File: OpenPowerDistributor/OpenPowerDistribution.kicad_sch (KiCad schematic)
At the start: 0 parts

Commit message: Started to draw schematic
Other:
- added sheet 24V boost (24V boost.kicad_sch)
- added sheet 3.3V internal supply (3.3V internal supply.kicad_sch)
- added sheet 30V Gate power (30V Gate power.kicad_sch)
- added sheet 5V buck converter (5V buck converter.kicad_sch)
- added sheet Power input (Power input.kicad_sch)
- note added: "30V power supply for high-side FET gate power"
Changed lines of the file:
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@@
 (kicad_sch (version 20230121) (generator eeschema)
   (paper "A4")
+  (text "30V power supply for high-side FET gate power" (at 54.61 24.13 0)
+    (effects (font (size 3 3)) (justify left bottom))
+  )
+  (sheet (at 77.47 52.07) (size 40.64 13.97) (fields_autoplaced)
+    (stroke (width 0.1524) (type solid))
+    (fill (color 0 0 0 0.0000))
+    (property "Sheetname" "24V boost" (at 77.47 51.3584 0)
+      (effects (font (size 1.27 1.27)) (justify left bottom))
+    )
+    (property "Sheetfile" "24V boost.kicad_sch" (at 77.47 66.6246 0)
+      (effects (font (size 1.27 1.27)) (justify left top))
+    )
+    (instances
+      (project "OpenPowerDistribution"
+        (path "/df87b081-37a2-452c-8581-7eff2c408a17" (page "6"))
+      )
+    )
+  )
+  (sheet (at 77.47 34.29) (size 40.64 11.43) (fields_autoplaced)
+    (stroke (width 0.1524) (type solid))
+    (fill (color 0 0 0 0.0000))
+    (property "Sheetname" "30V Gate power" (at 77.47 33.5784 0)
+      (effects (font (size 1.27 1.27)) (justify left bottom))
+    )
+    (property "Sheetfile" "30V Gate power.kicad_sch" (at 77.47 46.3046 0)
+      (effects (font (size 1.27 1.27)) (justify left top))
+    )
+    (instances
+      (project "OpenPowerDistribution"
+        (path "/df87b081-37a2-452c-8581-7eff2c408a17" (page "5"))
+      )
+    )
+  )
+  (sheet (at 77.47 93.98) (size 40.64 11.43) (fields_autoplaced)
+    (stroke (width 0.1524) (type solid))
+    (fill (color 0 0 0 0.0000))
+    (property "Sheetname" "3.3V internal supply" (at 77.47 93.2684 0)
+      (effects (font (size 1.27 1.27)) (justify left bottom))
+    )
+    (property "Sheetfile" "3.3V internal supply.kicad_sch" (at 77.47 105.9946 0)
+      (effects (font (size 1.27 1.27)) (justify left top))
+    )
+    (instances
+      (project "OpenPowerDistribution"
+        (path "/df87b081-37a2-452c-8581-7eff2c408a17" (page "4"))
+      )
+    )
+  )
+  (sheet (at 38.1 34.29) (size 29.21 11.43) (fields_autoplaced)
+    (stroke (width 0.1524) (type solid))
+    (fill (color 0 0 0 0.0000))
+    (property "Sheetname" "Power input" (at 38.1 33.5784 0)
+      (effects (font (size 1.27 1.27)) (justify left bottom))
+    )
+    (property "Sheetfile" "Power input.kicad_sch" (at 38.1 46.3046 0)
+      (effects (font (size 1.27 1.27)) (justify left top))
+    )
+    (instances
+      (project "OpenPowerDistribution"
+        (path "/df87b081-37a2-452c-8581-7eff2c408a17" (page "2"))
+      )
+    )
+  )
+  (sheet (at 77.47 73.66) (size 40.64 11.43) (fields_autoplaced)
+    (stroke (width 0.1524) (type solid))
+    (fill (color 0 0 0 0.0000))
+    (property "Sheetname" "5V buck converter" (at 77.47 72.9484 0)
+      (effects (font (size 1.27 1.27)) (justify left bottom))
+    )
+    (property "Sheetfile" "5V buck converter.kicad_sch" (at 77.47 85.6746 0)
+      (effects (font (size 1.27 1.27)) (justify left top))
+    )
+    (instances
+      (project "OpenPowerDistribution"
+        (path "/df87b081-37a2-452c-8581-7eff2c408a17" (page "3"))
+      )
+    )
+  )
   (sheet_instances
     (path "/" (page "1"))

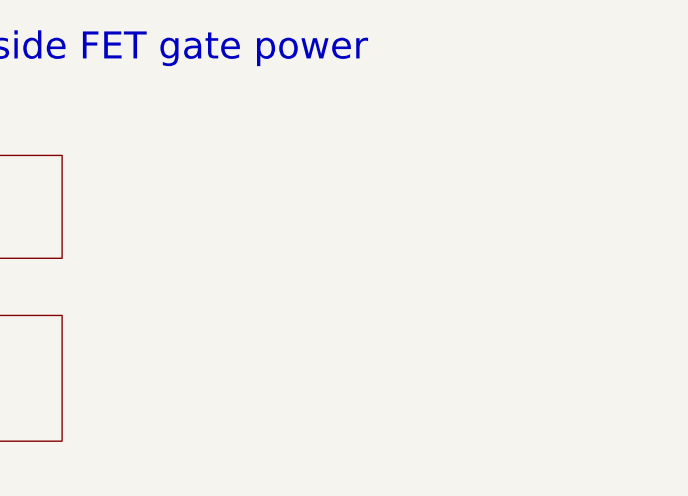
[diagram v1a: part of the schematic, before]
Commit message: Added manual high side power switch
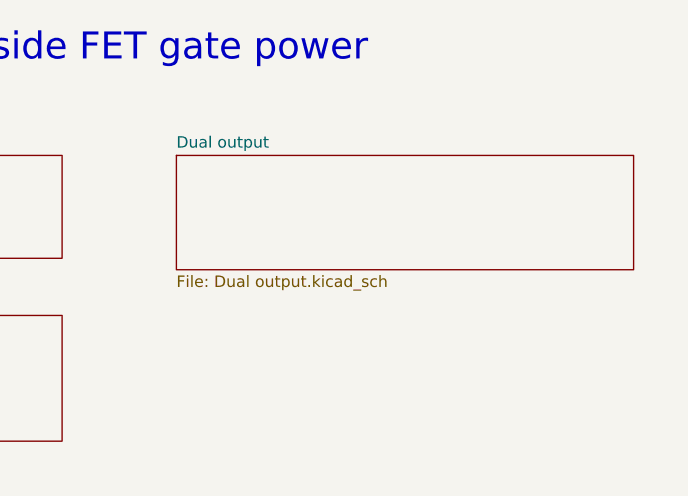
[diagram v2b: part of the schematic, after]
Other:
- added sheet Dual output (Dual output.kicad_sch)
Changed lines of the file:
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@@
+    )
+  )
+  (sheet (at 130.81 34.29) (size 50.8 12.7) (fields_autoplaced)
+    (stroke (width 0.1524) (type solid))
+    (fill (color 0 0 0 0.0000))
+    (property "Sheetname" "Dual output" (at 130.81 33.5784 0)
+      (effects (font (size 1.27 1.27)) (justify left bottom))
+    )
+    (property "Sheetfile" "Dual output.kicad_sch" (at 130.81 47.5746 0)
+      (effects (font (size 1.27 1.27)) (justify left top))
+    )
+    (instances
+      (project "OpenPowerDistribution"
+        (path "/df87b081-37a2-452c-8581-7eff2c408a17" (page "7"))
+      )
     )
   )

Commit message: More schematic progress
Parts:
- added D2 (x4): SMAJ9.0A, Diode_SMD:D_SMA, symbol Diode:SMAJ12A
- added D2 (x6): SMAJ5.0A, Diode_SMD:D_SMA, symbol Diode:SMAJ12A
- added D2 (x6): SMAJ12A, Diode_SMD:D_SMA, symbol Diode:SMAJ12A
- added D2 (x2): SMAJ24A, Diode_SMD:D_SMA, symbol Diode:SMAJ12A
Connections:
- new net Dual output/O1+: D2.1 (A1)
- new net Dual output/O1-: D2.2 (A2)
- new net Dual output/O2+: D2.1 (A1)
- new net Dual output/O2-: D2.2 (A2)
- new net Dual output1/O1+: D2.1 (A1)
- new net Dual output1/O1-: D2.2 (A2)
- new net Dual output1/O2+: D2.1 (A1)
- new net Dual output1/O2-: D2.2 (A2)
- new net Dual output2/O1+: D2.1 (A1)
- new net Dual output2/O1-: D2.2 (A2)
- new net Dual output2/O2+: D2.1 (A1)
- new net Dual output2/O2-: D2.2 (A2)
- new net Dual output3/O1+: D2.1 (A1)
- new net Dual output3/O1-: D2.2 (A2)
- new net Dual output3/O2+: D2.1 (A1)
- new net Dual output3/O2-: D2.2 (A2)
- new net Dual output4/O1+: D2.1 (A1)
- new net Dual output4/O1-: D2.2 (A2)
- new net Dual output4/O2+: D2.1 (A1)
- new net Dual output4/O2-: D2.2 (A2)
- new net Dual output5/O1+: D2.1 (A1)
- new net Dual output5/O1-: D2.2 (A2)
- new net Dual output5/O2+: D2.1 (A1)
- new net Dual output5/O2-: D2.2 (A2)
- new net Dual output6/O1+: D2.1 (A1)
- new net Dual output6/O1-: D2.2 (A2)
- new net Dual output6/O2+: D2.1 (A1)
- new net Dual output6/O2-: D2.2 (A2)
- new net Dual output7/O1+: D2.1 (A1)
- new net Dual output7/O1-: D2.2 (A2)
- new net Dual output7/O2+: D2.1 (A1)
- new net Dual output7/O2-: D2.2 (A2)
- new net Dual output8/O1+: D2.1 (A1)
- new net Dual output8/O1-: D2.2 (A2)
- new net Dual output8/O2+: D2.1 (A1)
- new net Dual output8/O2-: D2.2 (A2)
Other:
- added sheet 9V buck converter (9V buck converter.kicad_sch)
- added sheet Dual output1 (Dual output.kicad_sch)
- added sheet Dual output2 (Dual output.kicad_sch)
- added sheet Dual output3 (Dual output.kicad_sch)
- added sheet Dual output4 (Dual output.kicad_sch)
- added sheet Dual output5 (Dual output.kicad_sch)
- added sheet Dual output6 (Dual output.kicad_sch)
- added sheet Dual output7 (Dual output.kicad_sch)
- added sheet Dual output8 (Dual output.kicad_sch)
- sheet Dual output ports: added Iset1, Iset2, Isns1, Isns2, O1+, O1-, O2+, O2-, V_{In}, ~{Overcurrent}1, ~{Overcurrent}2; removed none
- note added: "Dual 24V output"
- note added: "Hex 12V output"
- note added: "Hex 5V output"
- note added: "Quad 9V output"

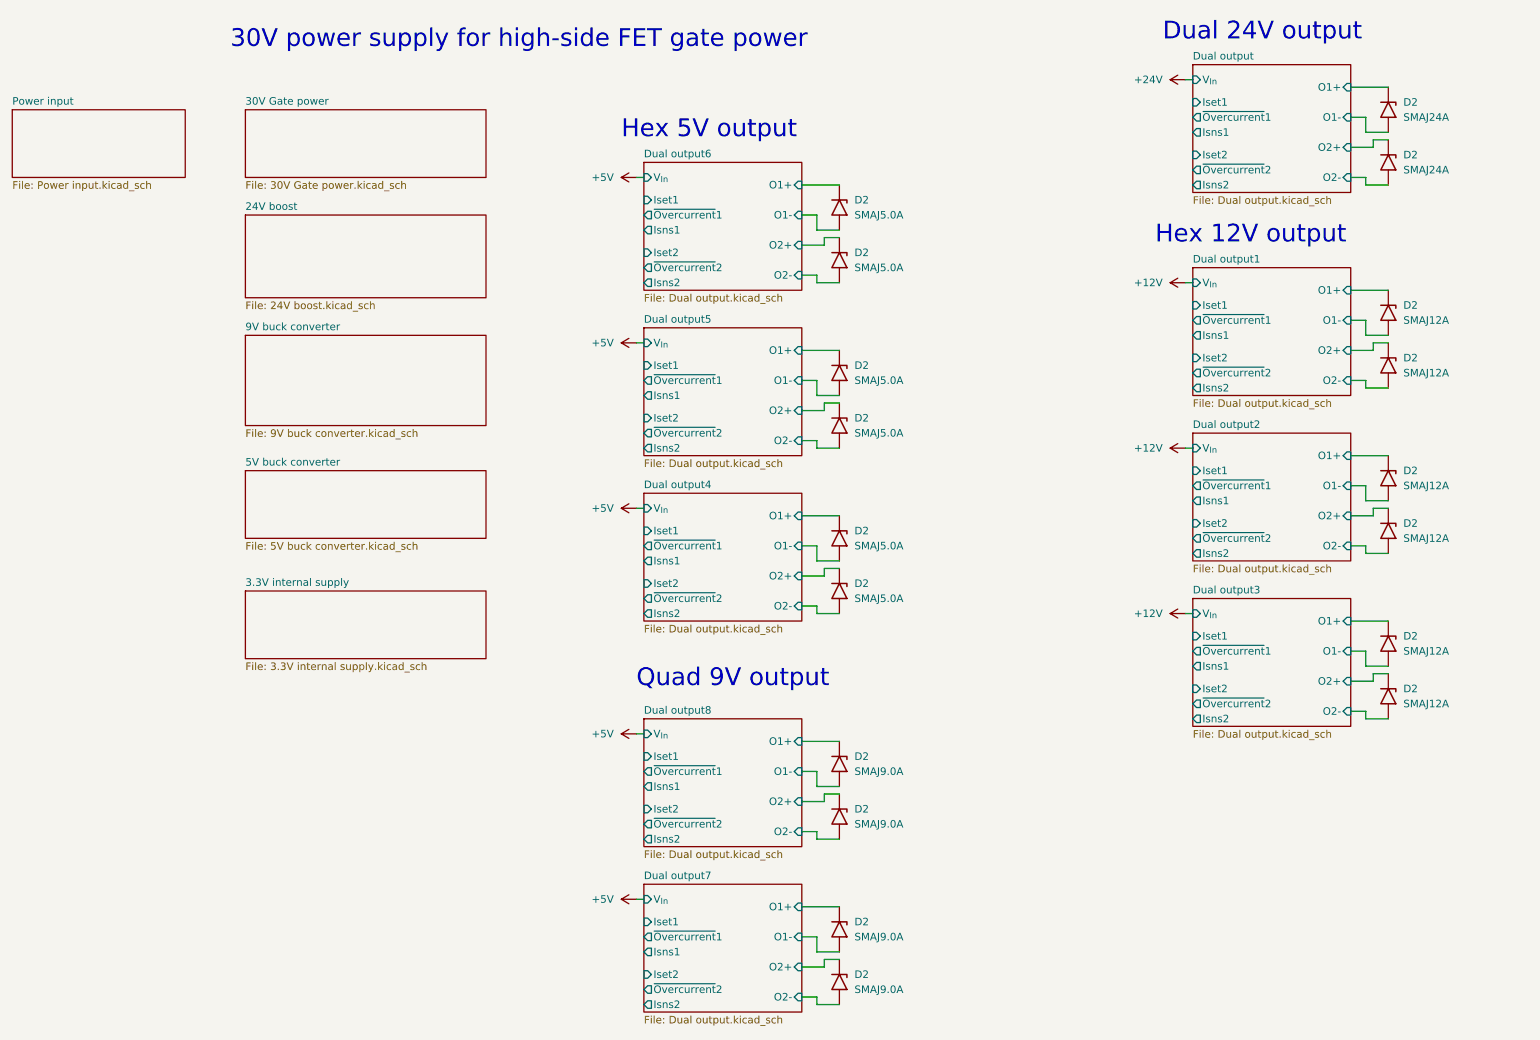
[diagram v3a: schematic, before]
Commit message: More work on schematic wiring
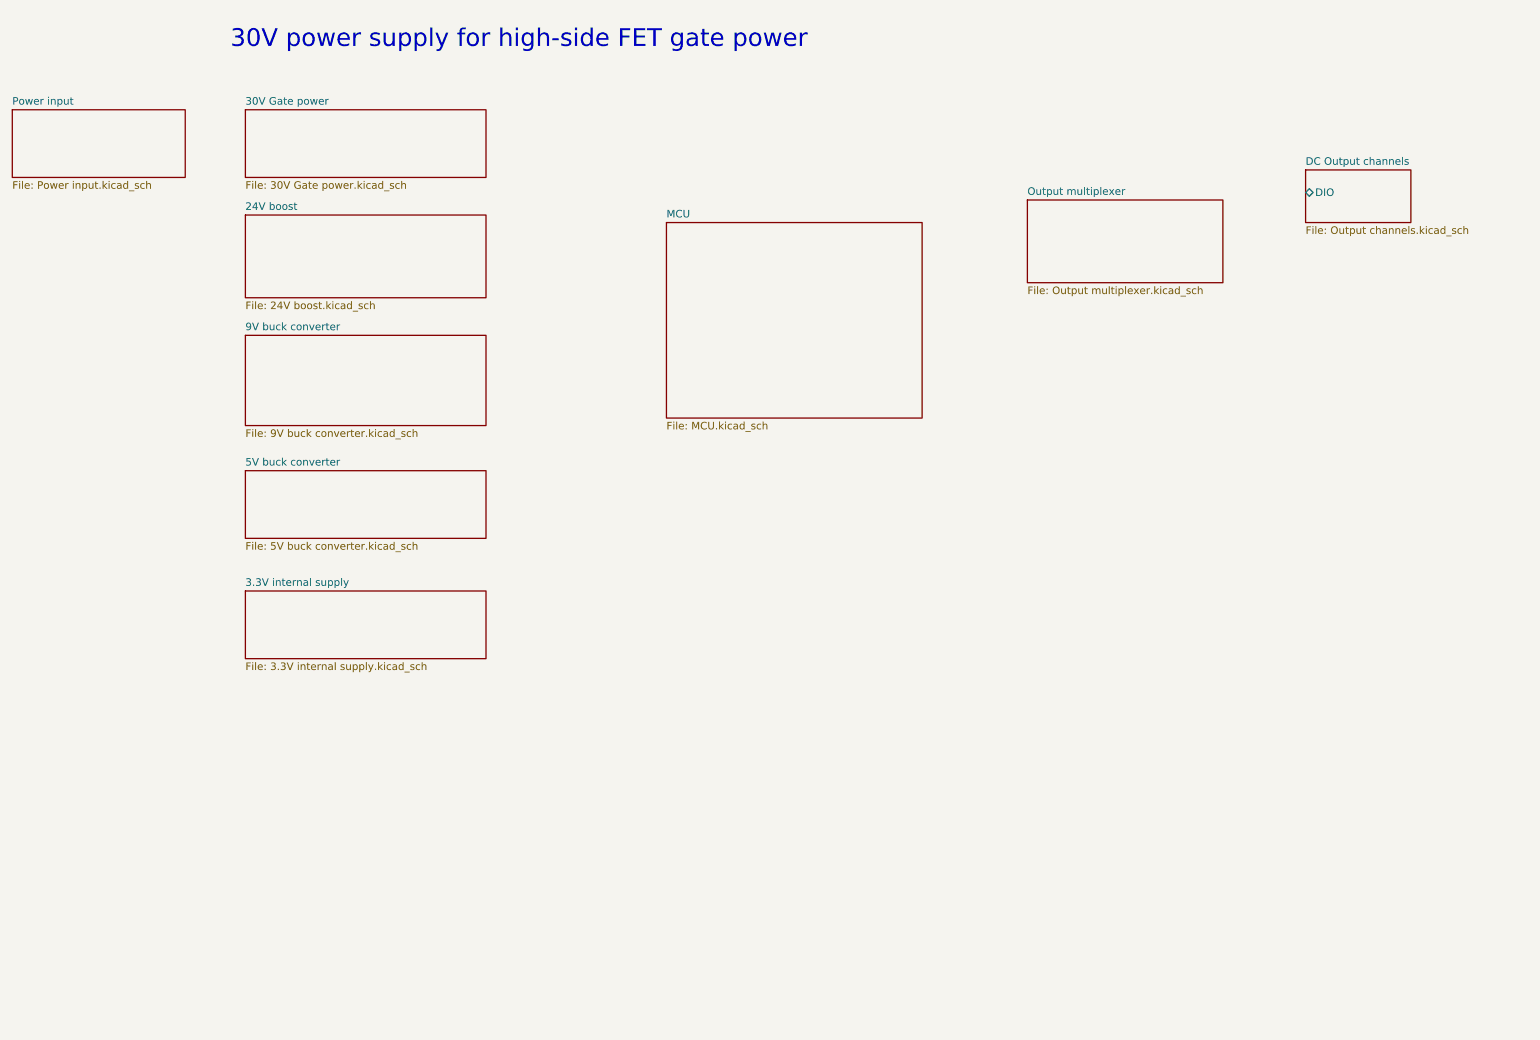
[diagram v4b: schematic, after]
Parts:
- removed D2 (x4): SMAJ9.0A, Diode_SMD:D_SMA, symbol Diode:SMAJ12A
- removed D2 (x6): SMAJ5.0A, Diode_SMD:D_SMA, symbol Diode:SMAJ12A
- removed D2 (x6): SMAJ12A, Diode_SMD:D_SMA, symbol Diode:SMAJ12A
- removed D2 (x2): SMAJ24A, Diode_SMD:D_SMA, symbol Diode:SMAJ12A
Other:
- removed sheet Dual output
- removed sheet Dual output1
- removed sheet Dual output2
- removed sheet Dual output3
- removed sheet Dual output4
- removed sheet Dual output5
- removed sheet Dual output6
- removed sheet Dual output7
- removed sheet Dual output8
- added sheet DC Output channels (Output channels.kicad_sch)
- added sheet MCU (MCU.kicad_sch)
- added sheet Output multiplexer (Output multiplexer.kicad_sch)
- note removed: "Dual 24V output"
- note removed: "Hex 12V output"
- note removed: "Hex 5V output"
- note removed: "Quad 9V output"

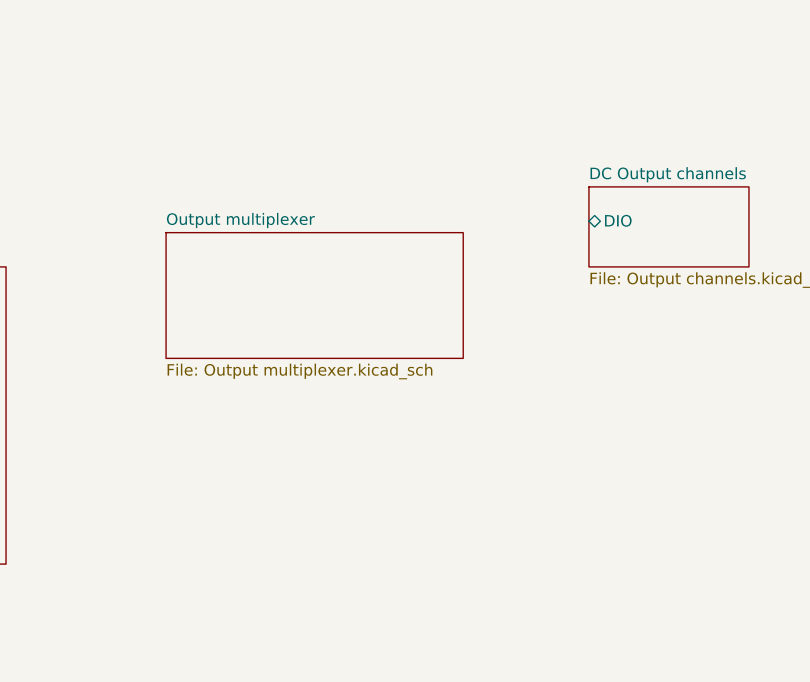
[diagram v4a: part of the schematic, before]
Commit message: Start to make layout
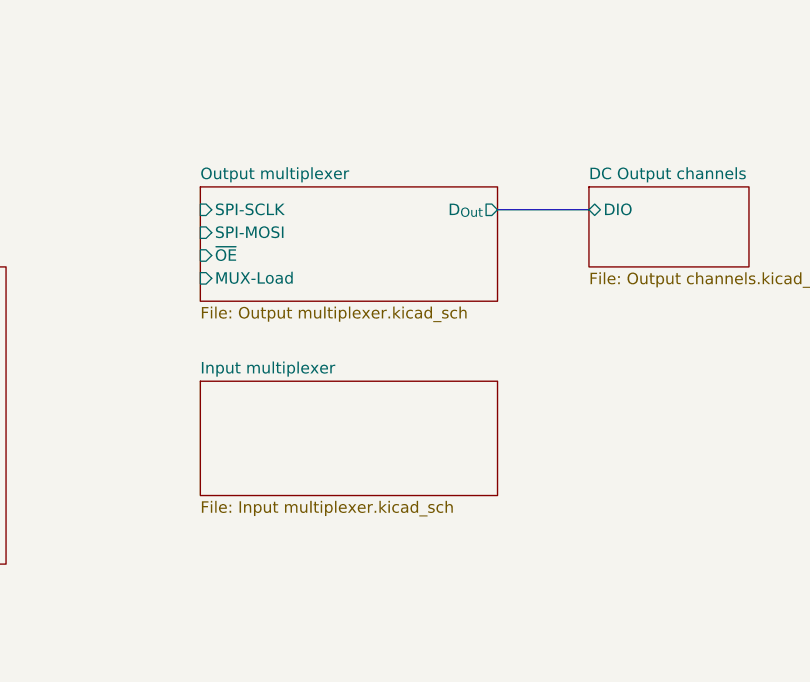
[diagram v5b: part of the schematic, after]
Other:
- added sheet Input multiplexer (Input multiplexer.kicad_sch)
- sheet Output multiplexer ports: added D_{Out}, MUX-Load, SPI-MOSI, SPI-SCLK, ~{OE}; removed none
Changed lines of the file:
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@@
 (kicad_sch (version 20230121) (generator eeschema)
   (paper "A4")
+  (bus (pts (xy 226.06 46.99) (xy 236.22 46.99))
+    (stroke (width 0) (type default))
+  )
   (text "30V power supply for high-side FET gate power" (at 54.61 24.13 0)
     (effects (font (size 3 3)) (justify left bottom))
@@
       (effects (font (size 1.27 1.27)) (justify left top))
     )
-    (pin "DIO" bidirectional (at 236.22 48.26 180)
+    (pin "DIO" bidirectional (at 236.22 46.99 180)
       (effects (font (size 1.27 1.27)) (justify left))
     )
@@
     )
   )
-  (sheet (at 189.23 49.53) (size 33.02 13.97) (fields_autoplaced)
+  (sheet (at 193.04 44.45) (size 33.02 12.7) (fields_autoplaced)
     (stroke (width 0.1524) (type solid))
     (fill (color 0 0 0 0.0000))
-    (property "Sheetname" "Output multiplexer" (at 189.23 48.8184 0)
+    (property "Sheetname" "Output multiplexer" (at 193.04 43.7384 0)
       (effects (font (size 1.27 1.27)) (justify left bottom))
     )
-    (property "Sheetfile" "Output multiplexer.kicad_sch" (at 189.23 64.0846 0)
+    (property "Sheetfile" "Output multiplexer.kicad_sch" (at 193.04 57.7346 0)
       (effects (font (size 1.27 1.27)) (justify left top))
+    )
+    (pin "D_{Out}" output (at 226.06 46.99 0)
+      (effects (font (size 1.27 1.27)) (justify right))
+    )
+    (pin "SPI-SCLK" input (at 193.04 46.99 180)
+      (effects (font (size 1.27 1.27)) (justify left))
+    )
+    (pin "SPI-MOSI" input (at 193.04 49.53 180)
+      (effects (font (size 1.27 1.27)) (justify left))
+    )
+    (pin "~{OE}" input (at 193.04 52.07 180)
+      (effects (font (size 1.27 1.27)) (justify left))
+    )
+    (pin "MUX-Load" input (at 193.04 54.61 180)
+      (effects (font (size 1.27 1.27)) (justify left))
     )
     (instances
@@
       )
     )
+  )
+  (sheet (at 193.04 66.04) (size 33.02 12.7) (fields_autoplaced)
+    (stroke (width 0.1524) (type solid))
+    (fill (color 0 0 0 0.0000))
+    (property "Sheetname" "Input multiplexer" (at 193.04 65.3284 0)
+      (effects (font (size 1.27 1.27)) (justify left bottom))
+    )
+    (property "Sheetfile" "Input multiplexer.kicad_sch" (at 193.04 79.3246 0)
+      (effects (font (size 1.27 1.27)) (justify left top))
+    )
+    (instances
+      (project "OpenPowerDistribution"
+        (path "/df87b081-37a2-452c-8581-7eff2c408a17" (page "20"))
+      )
+    )
